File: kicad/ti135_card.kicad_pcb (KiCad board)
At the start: 8 copper layers, 76 x 65.1 mm, 293 parts, among them J1 JTAG 3.3V, J2 UART 3.3V, J3 2x19 1.27mm socket (bottom), J5 LCD 1x14 2.54mm, J6 2x3 1.27mm (bottom), J9 HR911130A, U1001 THGAMVG7T13BAIL, U101 NCP163ASN330T1G, U1201 SN74AXC8T245PWR, U1202 SN74AXC8T245PWR, U1203 SN74AXC8T245PWR, U1204 SN74AXC8T245PWR, U1301 SN74LV4051APWR, U1302 OPA365AIDBVR, U1303 ADS7056IRUGR, U201 TLV62585PDRLR, U301 TLV62585PDRLR, U311 TLV62585PDRLR, U331 TLV62585PDRLR, U341 TLV62585PDRLR, U401 TPS3808G01DBVR, U501 Ti135N484I3, U601 IS25WP128-RHLE, U801 H9HCNNN8KUMLHR-NME, U901 RTL8211FDI-CG, U902 74LVC1G07GW, Y701 SiT8924BA-73-18N-25.000000, Y901 25MHz

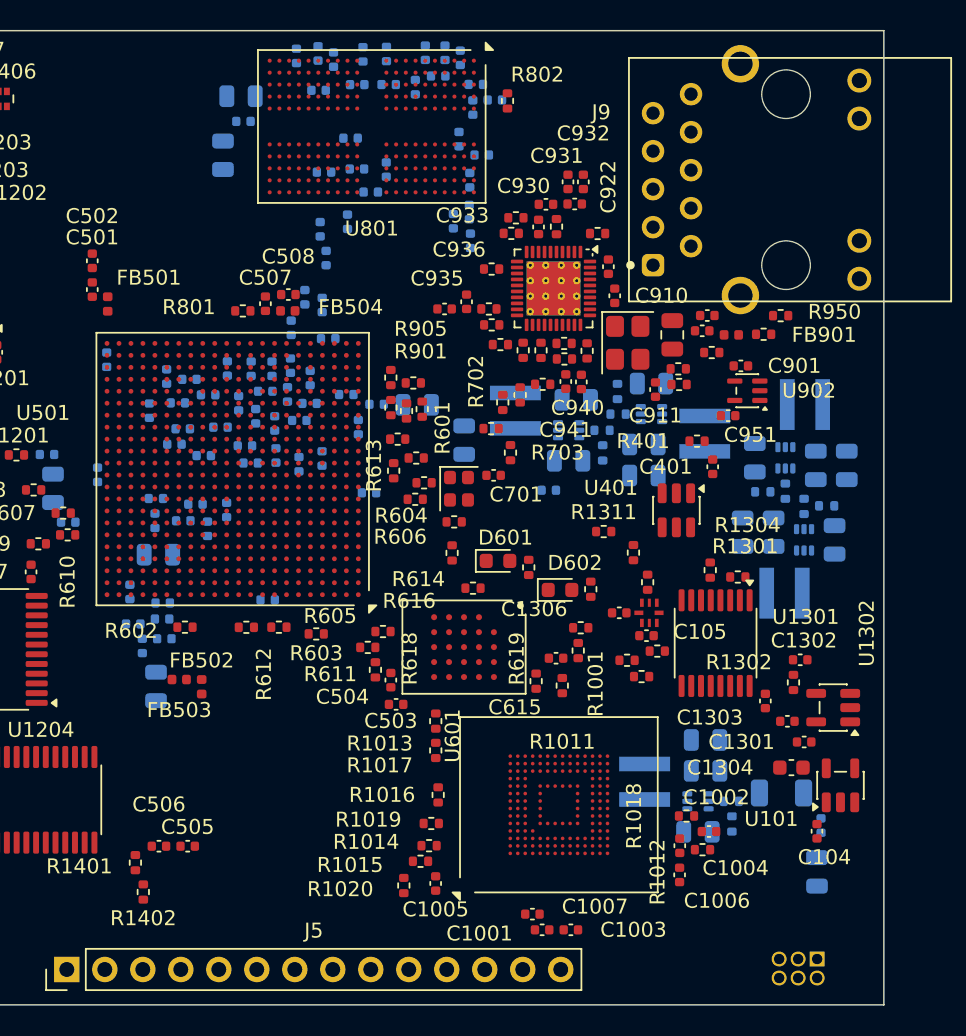
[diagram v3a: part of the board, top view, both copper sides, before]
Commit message: Planes and via-in-pad BGA fan-out
- Plane regions are drawn by script (tools/plane_regions.py -> placement/planes.json ->
  tools/apply_planes.py): In1/In6 GND; In3 1V1 north + VCORE corridor + GND; In4 1V8 with a
  0V85 island; B.Cu 5V0 region around J6 and the regulator inputs. Inside U501 each ball-grid
  cell goes to the nearest supply ball. 3V3 is routed rather than poured. route_planes' Voronoi
  split had cut VCORE off from its regulator.
- Via-in-pad on every connected ball (tools/via_in_pad.py): U501 392 x 0.30/0.15 mm,
  U801 178 x 0.25/0.15 mm. All 334 plane balls lie inside their plane's fill.
- Under-BGA decaps moved off the vias (place_fanout_clearance, 69 caps, no via nudges);
  3 nudged 0.05 mm for hole clearance.
- DRC: no clearance or hole errors, schematic parity 0. Test: LPDDR4 byte 1 routes 9/11 on In2.

Co-Authored-By: Claude Opus 5.5 <noreply@anthropic.com>
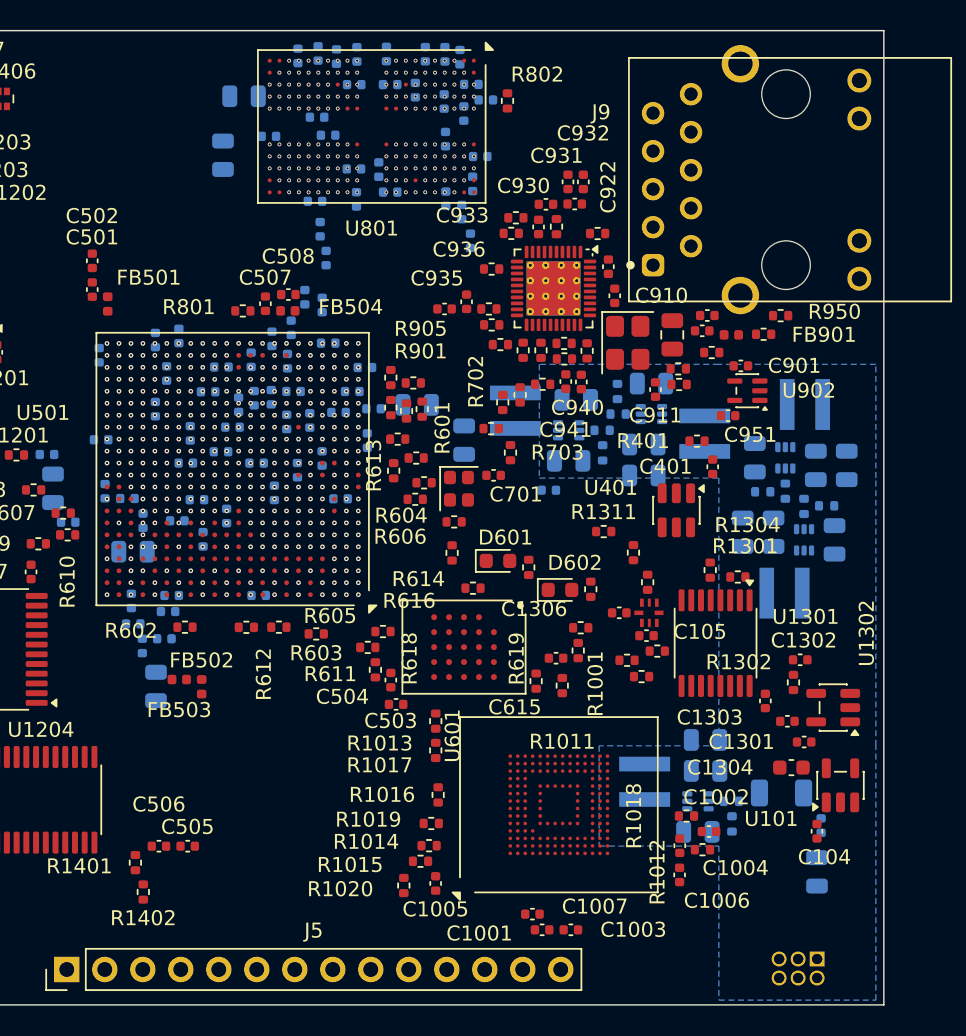
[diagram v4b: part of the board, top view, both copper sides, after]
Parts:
- moved C557 4.91 mm to (155.2, 79.0)
- moved C560 4.46 mm to (158.8, 72.4), turned to -90 degrees
- moved C529 4.41 mm to (172.8, 74.2), turned to 180 degrees
- moved C540 2.98 mm to (160.4, 72.1), turned to -90 degrees
- moved C549 2.98 mm to (171.1, 77.2), turned to 180 degrees
- moved C558 2.50 mm to (166.8, 82.6)
- moved C828 2.04 mm to (169.5, 63.1)
- moved C546 2.00 mm to (166.6, 72.3), turned to -90 degrees
- moved C835 1.97 mm to (166.4, 58.8)
- moved C563 1.94 mm to (171.2, 83.0)
- moved C555 1.90 mm to (157.0, 83.0)
- moved C809 1.80 mm to (169.6, 57.5)
- moved C818 1.75 mm to (178.1, 56.4), turned to 90 degrees
- moved C509 1.71 mm to (157.3, 86.5)
- moved C522 1.65 mm to (163.2, 79.8)
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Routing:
- net VCORE: vias 0 -> 36
- net Net-(U801B-ZQ0): vias 0 -> 1
- net Net-(U501F-REF_RES_4B): vias 0 -> 1
- net Net-(U501F-REF_RES_4A): vias 0 -> 1
- net Net-(U501F-REF_RES_2C): vias 0 -> 1
- net Net-(U501F-REF_RES_2A): vias 0 -> 1
- net Net-(U501A-DDR_CAL): vias 0 -> 1
- net GND: vias 0 -> 190
- net 3V3: vias 0 -> 3
- net 1V8: vias 0 -> 23
- net 1V1: vias 0 -> 70
- net 0V85: vias 0 -> 15
- net /uart_tx: vias 0 -> 1
- net /uart_rx: vias 0 -> 1
- net /t_irq: vias 0 -> 1
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- added copper zone on In4.Cu, net 0V85
- added copper zone on In3.Cu, net 1V1
- added copper zone on In4.Cu, net 1V8
- added copper zone on B.Cu, net 5V0
- added copper zone on In1.Cu, net GND
- added copper zone on In3.Cu, net GND
- added copper zone on In6.Cu, net GND
- added copper zone on In3.Cu, net VCORE

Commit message: Regulator cells: fix the bottom-side template mirror, draw the cell copper
- On B.Cu the template fit had mirrored every cell relative to its pins: CIN at the GND pin,
  COUT on the VIN side. placement/sketches_B holds mirrored sketches (prep.sh now uses them).
  The 37 power parts were re-placed with everything else locked, and each cell was verified
  against TI Figure 24 in the regulator's own frame.
- tools/buck_copper.py draws one cell layout through each cell's pad frame: SW, VIN, the GND
  strip with vias to In6, VOUT with vias to the rail plane, and FB. Every via is placed at the
  nearest site that clears foreign copper on all layers.
- DRC clean, apart from routing and silk; all cell nets connect except the 3V3 output and
  EN/PG, which are left to the router.

Co-Authored-By: Claude Opus 5.5 <noreply@anthropic.com>
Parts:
- moved R201 19.9 mm to (201.7, 103.2)
- moved R202 19.8 mm to (200.2, 103.2), turned to -90 degrees
- moved L331 16.5 mm to (199.4, 75.7), turned to 180 degrees
- moved C203 16.4 mm to (196.1, 101.5), turned to -90 degrees
- moved C202 16.4 mm to (198.1, 101.5), turned to -90 degrees
- moved C331 16.3 mm to (202.7, 79.2), turned to -90 degrees
- moved U201 15.4 mm to (200.2, 101.0), turned to -90 degrees
- moved C201 15.4 mm to (202.2, 101.0), turned to -90 degrees
- moved U331 14.3 mm to (200.7, 79.2), turned to -90 degrees
- moved R331 13.6 mm to (202.2, 81.5), turned to 180 degrees
- moved R332 12.4 mm to (200.7, 81.5), turned to -90 degrees
- moved C332 12.2 mm to (198.7, 79.7), turned to -90 degrees
- moved C303 11.9 mm to (197.1, 89.6)
- moved C301 9.84 mm to (203.2, 89.1)
- moved C302 9.67 mm to (199.1, 89.6)
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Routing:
- net GND: track 0.00 -> 57.8 mm, vias 190 -> 215
- net 1V8: track 0.00 -> 8.62 mm, vias 23 -> 26
- net 1V1: track 0.00 -> 8.59 mm, vias 70 -> 73
- net VCORE: track 0.00 -> 8.48 mm, vias 36 -> 39
- net 5V0: track 0.00 -> 7.79 mm
- net 3V3: track 0.00 -> 5.22 mm
- net 0V85: track 0.00 -> 4.83 mm, vias 15 -> 17
- net Net-(U311-SW): track 0.00 -> 2.85 mm
- net Net-(U341-SW): track 0.00 -> 2.85 mm
- net Net-(U331-SW): track 0.00 -> 2.85 mm
- net Net-(U301-SW): track 0.00 -> 2.85 mm
- net Net-(U201-SW): track 0.00 -> 2.85 mm
- net Net-(U341-FB): track 0.00 -> 2.15 mm
- net Net-(U331-FB): track 0.00 -> 2.15 mm
- net Net-(U311-FB): track 0.00 -> 2.15 mm
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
